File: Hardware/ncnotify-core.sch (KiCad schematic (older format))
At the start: 44 parts, among them J1 5-1634503-1, J2 TC2030-CTX, J3 USB4110-GF-A, Q1 NX3008NBKS, SW1 SW_Push, SW2 SW_Push, U1 STM32L422CBT6, U2 TLV71333PDBV, U3 USBLC6-2SC6, U4 USBLC6-2SC6, X1 SMTU1632-LF, Y1 Q13FC1350000400

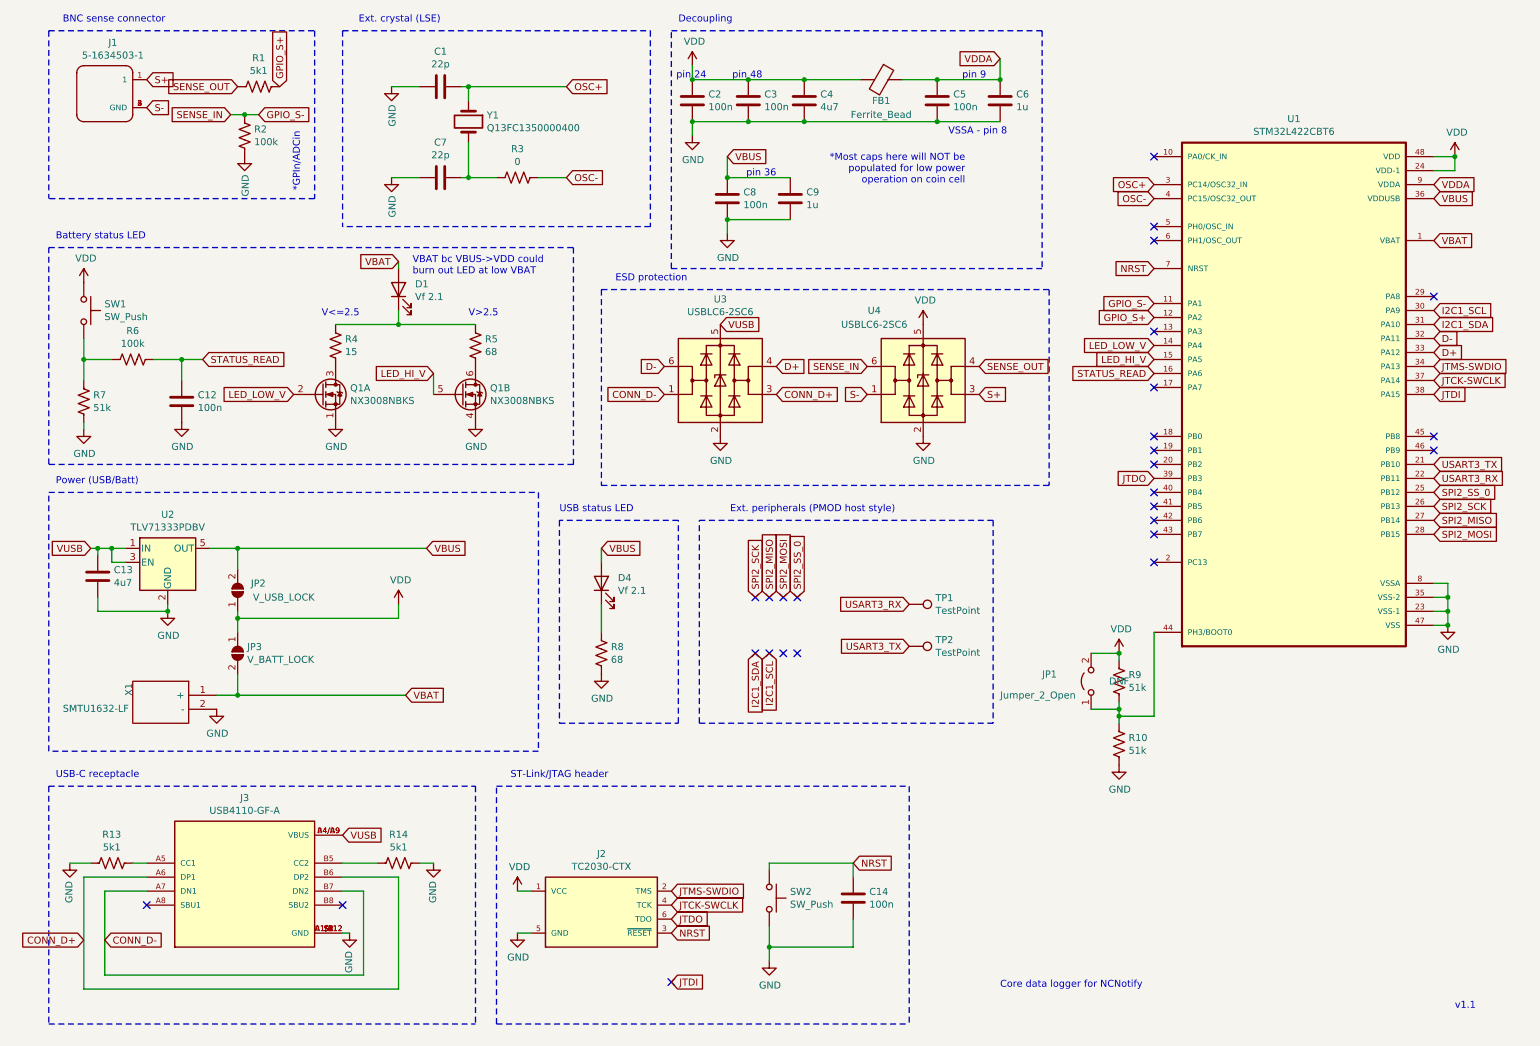
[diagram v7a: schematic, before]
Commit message: Board shrink; swap to RA BNC mount
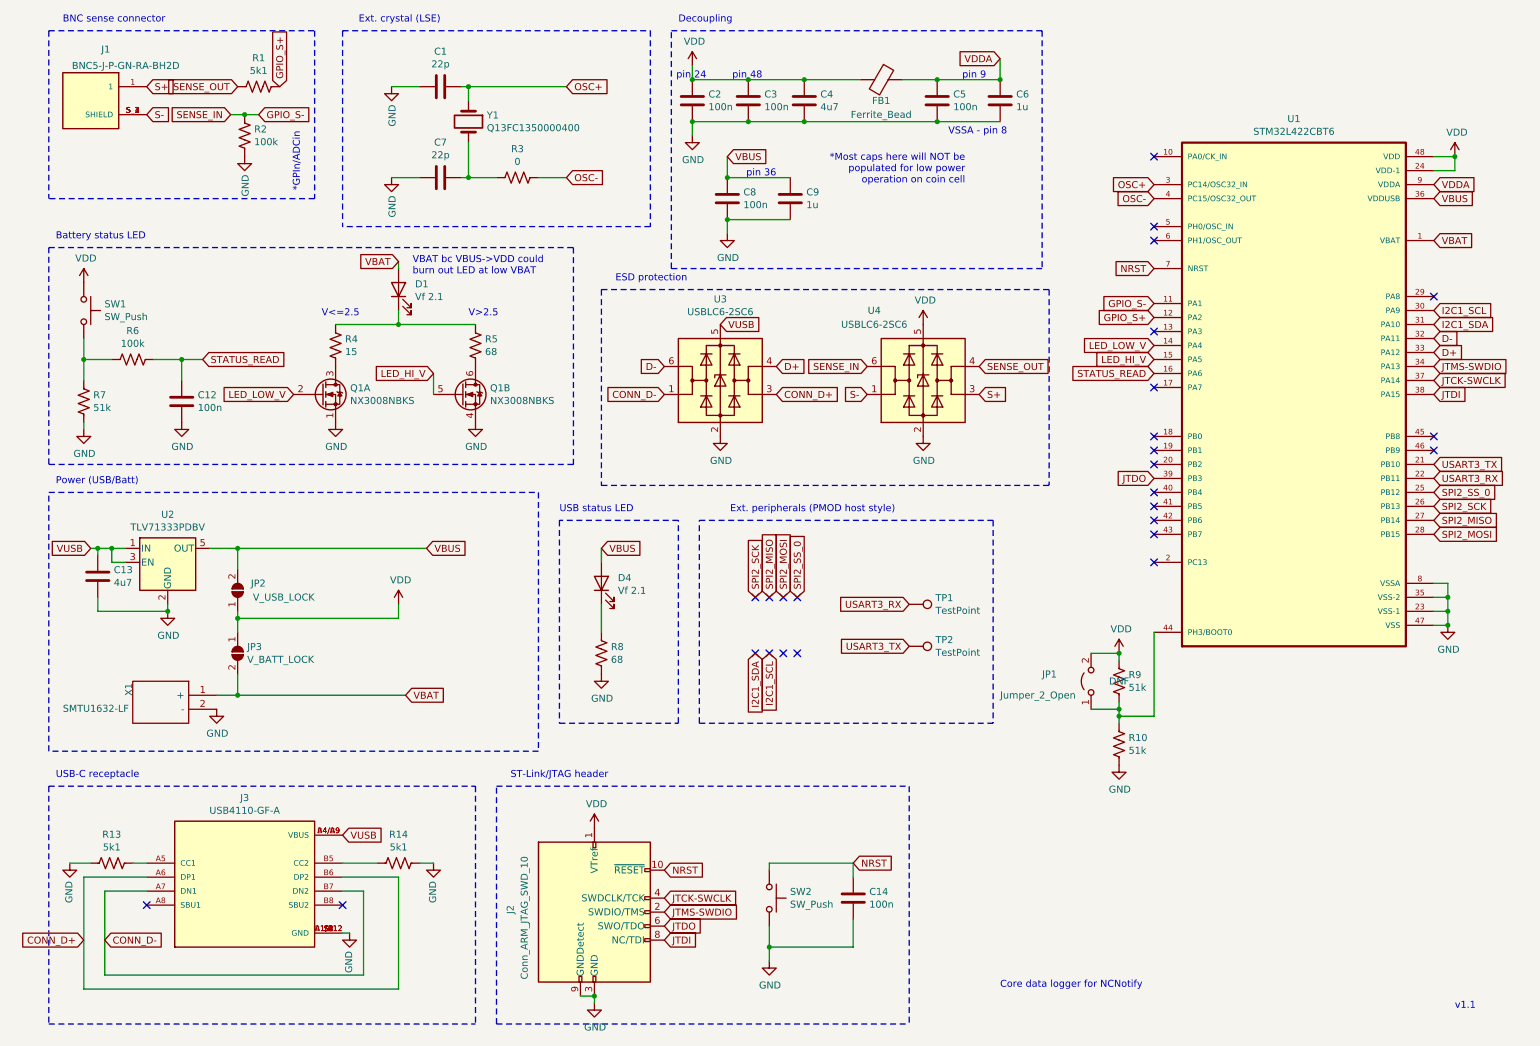
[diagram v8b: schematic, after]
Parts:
- removed J1: 5-1634503-1, libs:TE_5-1634503-1, symbol 5-1634503-1:5-1634503-1
- removed J2: TC2030-CTX, libs:TC2030-IDC-NL, symbol TC2030-CTX:TC2030-CTX
- added J1: BNC5-J-P-GN-RA-BH2D, SAMTEC_BNC5-J-P-GN-RA-BH2D, symbol BNC5-J-P-GN-RA-BH2D:BNC5-J-P-GN-RA-BH2D
- added J2: Conn_ARM_JTAG_SWD_10, Connector_PinHeader_1.27mm:PinHeader_2x05_P1.27mm_Vertical, symbol Connector:Conn_ARM_JTAG_SWD_10
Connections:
- net GND: now also J2.3 (GND), J2.5 (GND), J2.9 (GNDDetect)
- net JTCK-SWCLK: now also J2.4 (SWDCLK/TCK)
- net JTDI: now also J2.8 (NC/TDI)
- net JTDO: now also J2.6 (SWO/TDO)
- net JTMS-SWDIO: now also J2.2 (SWDIO/TMS)
- net NRST: now also J2.10 (~RESET~)
- net S+: now also J1.1
- net S-: now also J1.S_1 (SHIELD), J1.S_2 (SHIELD), J1.S_3 (SHIELD), J1.S_4 (SHIELD)
- net VDD: now also J2.1 (VTref)
- no-connect marks 27 -> 26
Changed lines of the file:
@@
 	-1   0    0    -1
-$EndComp
-$Comp
-L 5-1634503-1:5-1634503-1 J1
-U 1 1 5FA9B29C
-P 1050 1100
-F 0 "J1" H 1108 1465 50  0000 C CNN
-F 1 "5-1634503-1" H 1108 1374 50  0000 C CNN
-F 2 "libs:TE_5-1634503-1" H 1050 1100 50  0001 L BNN
-F 3 "" H 1050 1100 50  0001 L BNN
-F 4 "Compliant" H 1050 1100 50  0001 L BNN "EU_RoHS_Compliance"
-F 5 "1" H 1050 1100 50  0001 L BNN "Number_of_Positions"
-F 6 "5-1634503-1" H 1050 1100 50  0001 L BNN "Comment"
-F 7 "" H 1050 1100 50  0001 C CNN "LCSC Part #"
-	1    1050 1100
-	1    0    0    -1
 $EndComp
 Text Notes 750  600  0    50   ~ 0
@@
 Wire Notes Line
 	650  650  2550 650
-Text GLabel 5100 6800 2    50   Input ~ 0
+Text GLabel 5050 6950 2    50   Input ~ 0
 JTMS-SWDIO
 Text GLabel 10550 3050 2    50   Input ~ 0
@@
 Text GLabel 10550 3150 2    50   Input ~ 0
 JTCK-SWCLK
-Text GLabel 5100 6900 2    50   Input ~ 0
+Text GLabel 5050 6850 2    50   Input ~ 0
 JTCK-SWCLK
 Text GLabel 10550 3250 2    50   Input ~ 0
 JTDI
-Text GLabel 5100 7000 2    50   Input ~ 0
+Text GLabel 5050 7050 2    50   Input ~ 0
 JTDO
 Text GLabel 8550 3850 0    50   Input ~ 0
@@
 L power:VDD #PWR026
 U 1 1 5FB3E2D3
-P 4000 6800
-F 0 "#PWR026" H 4000 6650 50  0001 C CNN
-F 1 "VDD" H 4015 6973 50  0000 C CNN
-F 2 "" H 4000 6800 50  0001 C CNN
-F 3 "" H 4000 6800 50  0001 C CNN
-	1    4000 6800
+P 4550 6350
+F 0 "#PWR026" H 4550 6200 50  0001 C CNN
+F 1 "VDD" H 4565 6523 50  0000 C CNN
+F 2 "" H 4550 6350 50  0001 C CNN
+F 3 "" H 4550 6350 50  0001 C CNN
+	1    4550 6350
 	1    0    0    -1
 $EndComp
@@
 L power:GND #PWR031
 U 1 1 5FB3FA87
-P 4000 7100
-F 0 "#PWR031" H 4000 6850 50  0001 C CNN
-F 1 "GND" H 4005 6927 50  0000 C CNN
-F 2 "" H 4000 7100 50  0001 C CNN
-F 3 "" H 4000 7100 50  0001 C CNN
-	1    4000 7100
-	1    0    0    -1
-$EndComp
-Wire Wire Line
-	4000 7100 4100 7100
+P 4550 7600
+F 0 "#PWR031" H 4550 7350 50  0001 C CNN
+F 1 "GND" H 4555 7427 50  0000 C CNN
+F 2 "" H 4550 7600 50  0001 C CNN
+F 3 "" H 4550 7600 50  0001 C CNN
+	1    4550 7600
+	1    0    0    -1
+$EndComp
 Wire Notes Line
 	3850 7750 3850 6050
@@
 Text GLabel 5450 2750 2    50   Input ~ 0
 VUSB
-Text GLabel 1350 1000 2    50   Input ~ 0
-S+
-Text GLabel 1350 1200 2    50   Input ~ 0
-S-
 Text GLabel 7300 3250 2    50   Input ~ 0
 S+
@@
 	1    0    0    -1
 $EndComp
-$Comp
-L TC2030-CTX:TC2030-CTX J2
-U 1 1 5FC452D4
-P 4600 6900
-F 0 "J2" H 4600 7267 50  0000 C CNN
-F 1 "TC2030-CTX" H 4600 7176 50  0000 C CNN
-F 2 "libs:TC2030-IDC-NL" H 4600 6900 50  0001 C CNN
-F 3 "" H 4600 6900 50  0001 L BNN
-F 4 "" H 4600 6900 50  0001 C CNN "LCSC Part #"
-	1    4600 6900
-	1    0    0    -1
-$EndComp
-Wire Wire Line
-	4000 6800 4100 6800
-Text GLabel 5100 7100 2    50   Input ~ 0
+Text GLabel 5050 6650 2    50   Input ~ 0
 NRST
 $Comp
@@
 Text GLabel 5050 3250 0    50   Input ~ 0
 CONN_D-
-Text GLabel 5100 7450 2    50   Input ~ 0
+Text GLabel 5050 7150 2    50   Input ~ 0
 JTDI
-NoConn ~ 5100 7450
 $Comp
 L power:VDD #PWR09
@@
 	0    1    1    0
 $EndComp
+$Comp
+L Connector:Conn_ARM_JTAG_SWD_10 J2
+U 1 1 5FCB1000
+P 4550 6950
+F 0 "J2" V 3950 7000 50  0000 R CNN
+F 1 "Conn_ARM_JTAG_SWD_10" V 4050 7350 50  0000 R CNN
+F 2 "Connector_PinHeader_1.27mm:PinHeader_2x05_P1.27mm_Vertical" H 4550 6950 50  0001 C CNN
+F 3 "http://infocenter.arm.com/help/topic/com.arm.doc.ddi0314h/DDI0314H_coresight_components_trm.pdf" V 4200 5700 50  0001 C CNN
+	1    4550 6950
+	1    0    0    -1
+$EndComp
+Wire Wire Line
+	4450 7550 4550 7550
+Wire Wire Line
+	4550 7600 4550 7550
+Connection ~ 4550 7550
+Text GLabel 1350 1250 2    50   Input ~ 0
+S-
+Text GLabel 1350 1050 2    50   Input ~ 0
+S+
+$Comp
+L BNC5-J-P-GN-RA-BH2D:BNC5-J-P-GN-RA-BH2D J1
+U 1 1 5FD45A24
+P 950 1150
+F 0 "J1" H 843 783 50  0000 C CNN
+F 1 "BNC5-J-P-GN-RA-BH2D" H 700 900 50  0000 C CNN
+F 2 "SAMTEC_BNC5-J-P-GN-RA-BH2D" H 950 1150 50  0001 L BNN
+F 3 "" H 950 1150 50  0001 L BNN
+F 4 "SAMTEC" H 950 1150 50  0001 L BNN "MANUFACTURER"
+F 5 "C" H 950 1150 50  0001 L BNN "PARTREV"
+F 6 "Manufacturer recommendations" H 950 1150 50  0001 L BNN "STANDARD"
+	1    950  1150
+	-1   0    0    1
+$EndComp
 $EndSCHEMATC
